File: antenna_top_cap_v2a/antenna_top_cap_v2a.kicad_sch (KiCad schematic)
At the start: 56 parts, among them IC1 PCT2075DP,118, J1 Battery Charge Bypass, J10 BM04B-SRSS-TB(LF)(SN), J12 BM04B-SRSS-TB(LF)(SN), J12 FC Board Connector, J14 BM04B-SRSS-TB(LF)(SN), J16 BM04B-SRSS-TB(LF)(SN), J19 EPS Board Connector, J2 EPS USB Bootselect Jumper, J20 FC USB Bootselect Jumper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

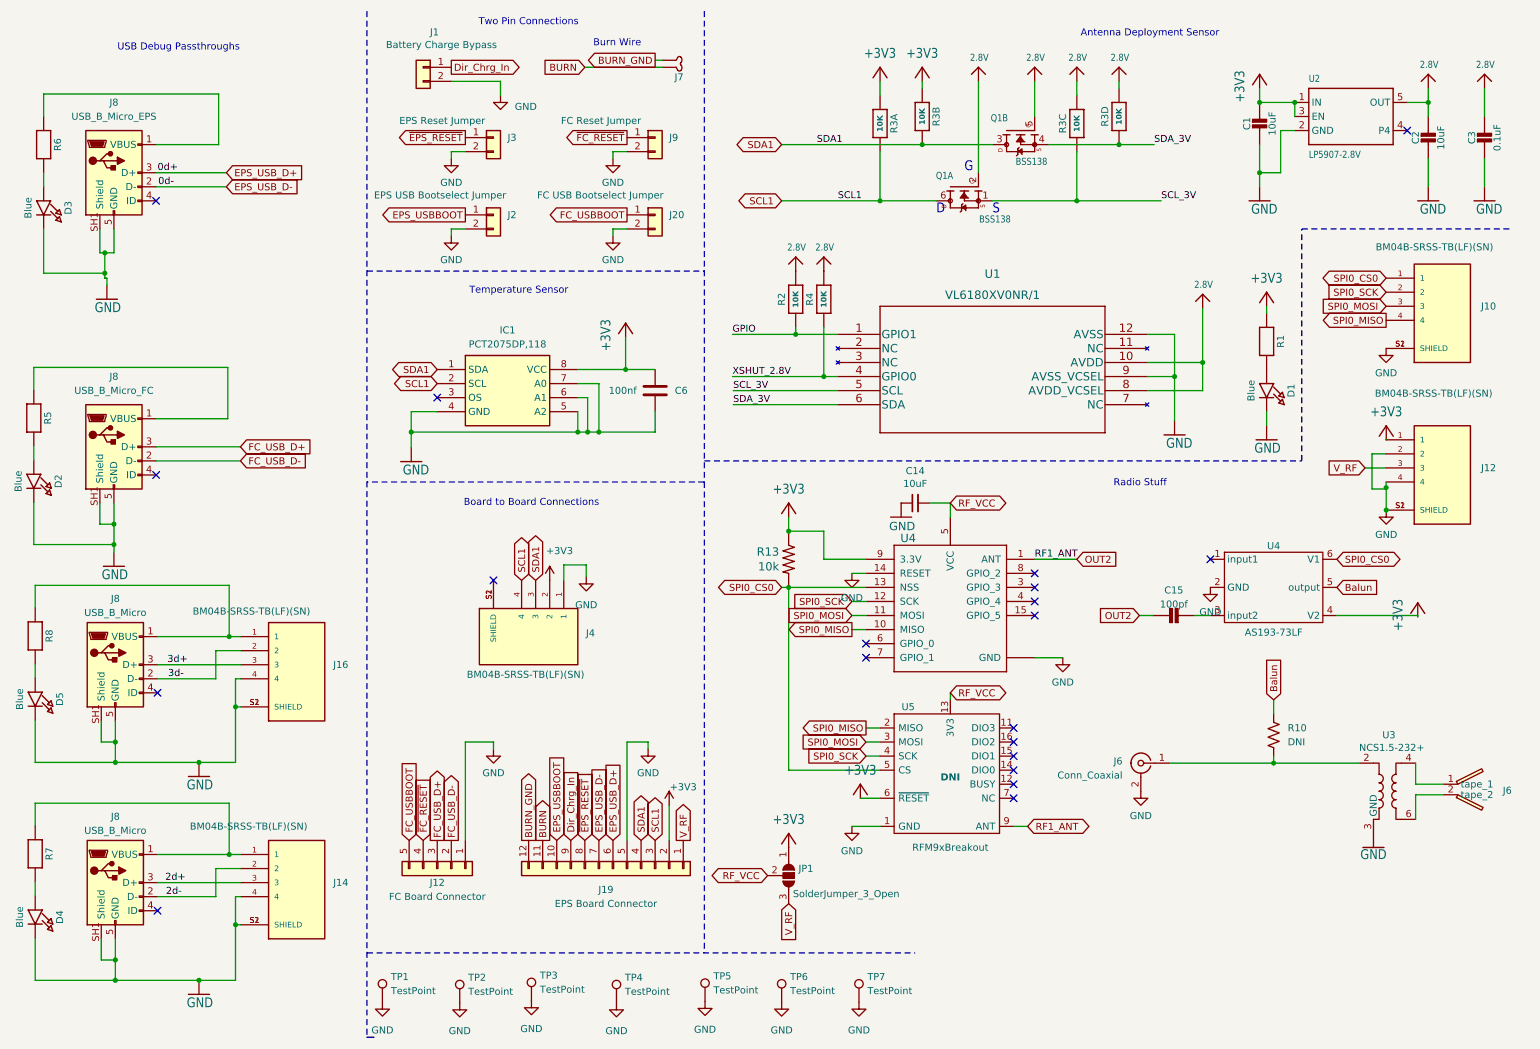
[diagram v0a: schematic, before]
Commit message: Deleted Unused Parts
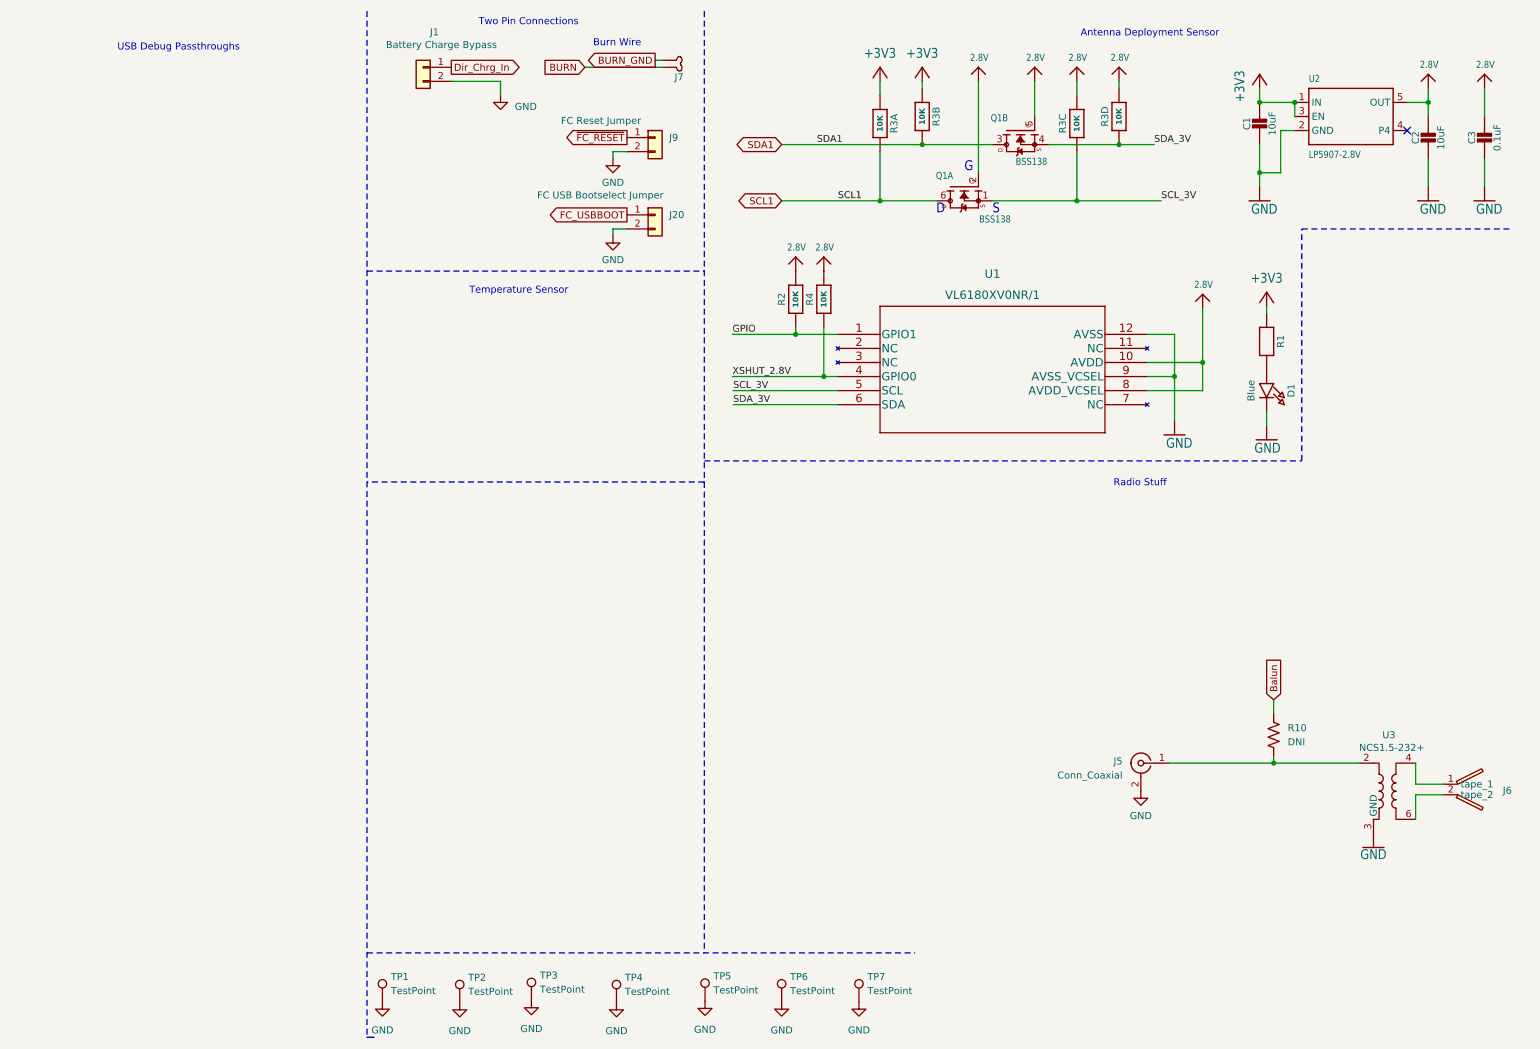
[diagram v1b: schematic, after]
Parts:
- removed C14: 10uF, Capacitor_SMD:C_0603_1608Metric, symbol Device:C_Small
- removed C15: 100pf, Capacitor_SMD:C_0603_1608Metric, symbol Adafruit ItsyBitsy RP2040-eagle-import:CAP_CERAMIC_0402NO
- removed C6: 100nf, Capacitor_SMD:C_0603_1608Metric, symbol Device:C
- removed D2, D3, D4, D5: Blue, LED_SMD:LED_0603_1608Metric, symbol Adafruit ItsyBitsy RP2040-eagle-import:LED0603_NOOUTLINE
- removed IC1: PCT2075DP,118, Package_SO:TSSOP-8_3x3mm_P0.65mm, symbol Antenna:PCT2075DP,118
- removed J10, J12, J14, J16, J4: BM04B-SRSS-TB(LF)(SN), Antenna_board:JST_BM04B-SRSS-TB(LF)(SN), symbol BM04B-SRSS-TB_LF__SN_:BM04B-SRSS-TB(LF)(SN)
- removed J12: FC Board Connector, FC_DEV_BOARD:MOLEX_5040500591, symbol Max_Lib:Connector_Generic_Conn_01x05
- removed J19: EPS Board Connector, Connector_Molex:Molex_Pico-Lock_504050-1291_1x12-1MP_P1.50mm_Horizontal, symbol Connector_Generic:Conn_01x12
- removed J2: EPS USB Bootselect Jumper, Connector_PinHeader_2.54mm:PinHeader_1x02_P2.54mm_Vertical, symbol Connector_Generic:Conn_01x02
- removed J3: EPS Reset Jumper, Connector_PinHeader_2.54mm:PinHeader_1x02_P2.54mm_Vertical, symbol Connector_Generic:Conn_01x02
- removed J8: USB_B_Micro_EPS, Antenna_board:MOLEX_105164-0001(round), symbol Connector:USB_B_Micro
- removed J8 (x2): USB_B_Micro, Antenna_board:MOLEX_105164-0001(round), symbol Connector:USB_B_Micro
- removed J8: USB_B_Micro_FC, Antenna_board:MOLEX_105164-0001(round), symbol Connector:USB_B_Micro
- removed JP1: SolderJumper_3_Open, Jumper:SolderJumper-3_P1.3mm_Open_RoundedPad1.0x1.5mm_NumberLabels, symbol Jumper:SolderJumper_3_Open
- removed R13: 10k, Resistor_SMD:R_0603_1608Metric, symbol mainboard:10KOHM-1_10W-1%(0603)0603
- removed R5, R6, R7, R8: 1K, Resistor_SMD:R_0402_1005Metric, symbol Adafruit ItsyBitsy RP2040-eagle-import:RESISTOR_0402NO
- removed U4: AS193-73LF, Package_TO_SOT_SMD:SuperSOT-6, symbol Antenna:RF_Switch
- removed U4: RFM98PW, Antenna_board:RFM98PW, symbol mainboard:RFM98PW
- removed U5: RFM9xBreakout, Antenna_board:HOPERF_RFM95W_SMD, symbol mainboard:RFM9xBreakout
- R1: value 1K -> 10k
- renumbered J6 to J5
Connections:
- no-connect marks 20 -> 1
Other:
- note removed: "Board to Board Connections"

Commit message: Added USB and DF11 Debug Connector
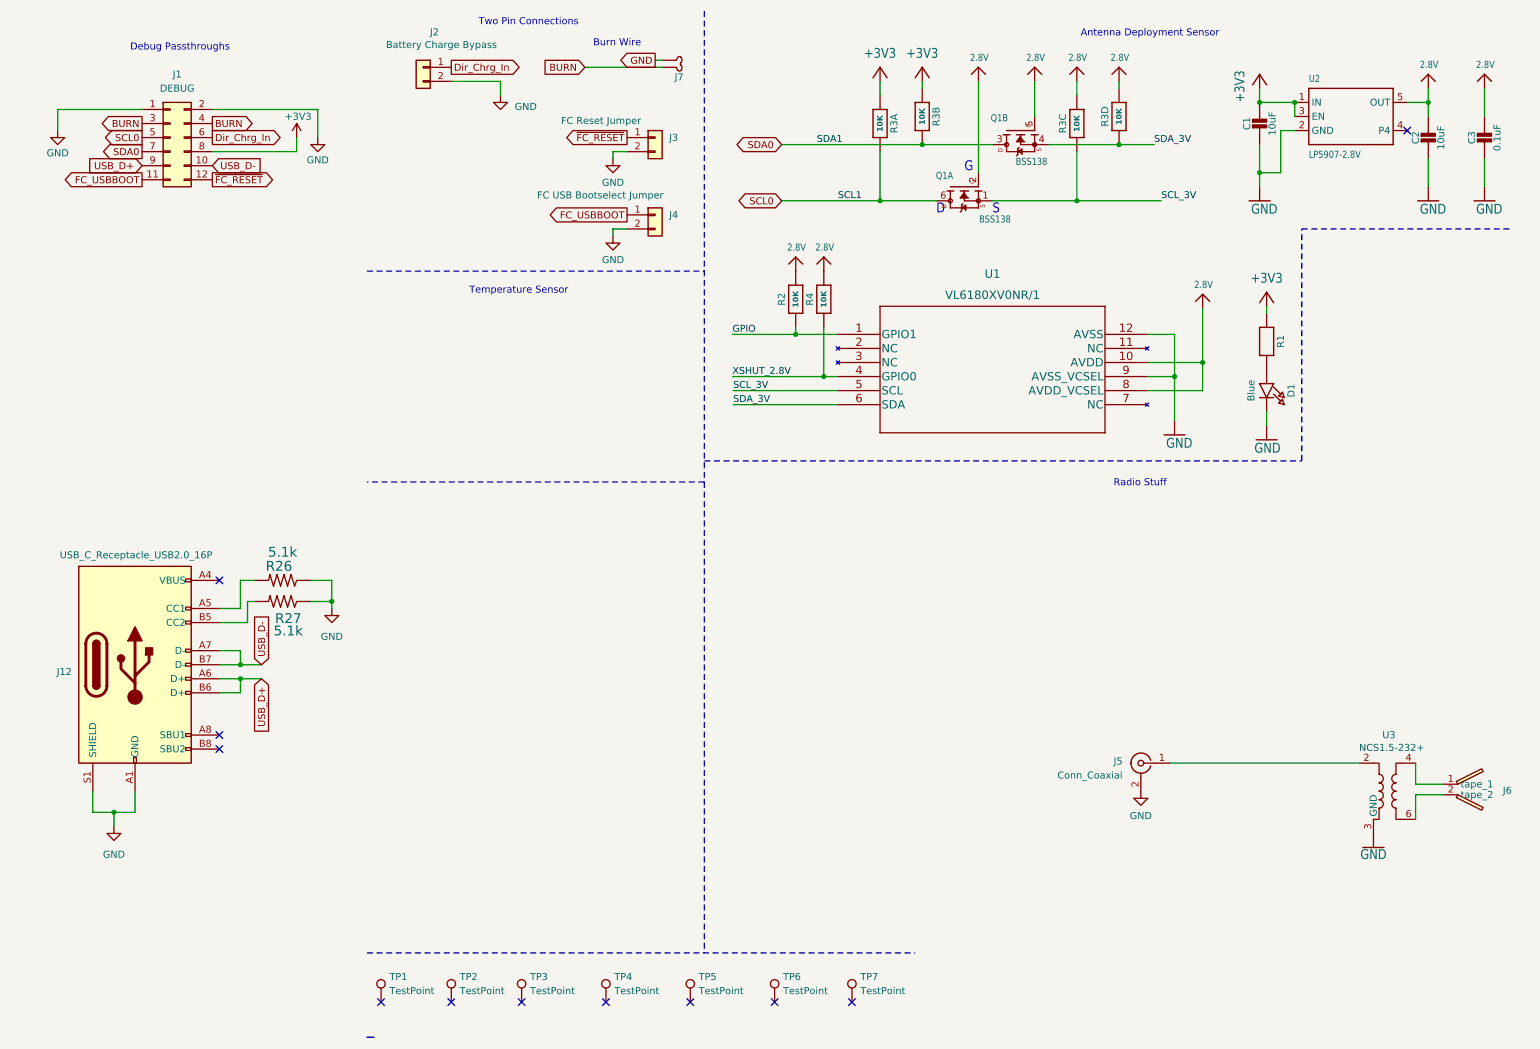
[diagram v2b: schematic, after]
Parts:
- removed R10: DNI, Resistor_SMD:R_0603_1608Metric, symbol Device:R_US
- added J1: DEBUG, Connector_Hirose:Hirose_DF11-12DP-2DSA_2x06_P2.00mm_Vertical, symbol Connector_Generic:Conn_02x06_Odd_Even
- added J12: USB_C_Receptacle_USB2.0_16P, Connector_USB:USB_C_Receptacle_HRO_TYPE-C-31-M-12, symbol Connector:USB_C_Receptacle_USB2.0_16P
- added R26, R27: 5.1k, Resistor_SMD:R_0603_1608Metric, symbol mainboard:RESISTOR0603
- renumbered J1 to J2, J9 to J3, J20 to J4
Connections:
- net BURN_GND is gone; now on net GND: J7.2 (GND)
- net +3V3: now also J1.8 (Pin_8)
- net BURN: now also J1.3 (Pin_3), J1.4 (Pin_4)
- net Dir_Chrg_In: now also J1.6 (Pin_6)
- net FC_USBBOOT: now also J1.11 (Pin_11)
- net GND: now also J1.1 (Pin_1), J1.2 (Pin_2), J12.A1 (GND), J12.A12 (GND), J12.B1 (GND), J12.B12 (GND), J12.S1 (SHIELD), R26.1, R27.1; no longer TP1.1, TP2.1, TP3.1, TP4.1, TP5.1, TP6.1, TP7.1
- net ~{FC_RESET}: now also J1.12 (Pin_12)
- net SCL1 renamed SCL0
- net SCL0: now also J1.5 (Pin_5)
- net SDA1 renamed SDA0
- net SDA0: now also J1.7 (Pin_7)
- new net: J12.A4 (VBUS), J12.A9 (VBUS), J12.B4 (VBUS), J12.B9 (VBUS)
- new net: J12.A5 (CC1), R26.2
- new net: J12.B5 (CC2), R27.2
- new net USB_D+: J1.9 (Pin_9), J12.A6 (D+), J12.B6 (D+)
- new net USB_D-: J1.10 (Pin_10), J12.A7 (D-), J12.B7 (D-)
- no-connect marks 1 -> 11
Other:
- note added: "Debug Passthroughs"
- note removed: "USB Debug Passthroughs"
- moved on the sheet: TP2, TP3, TP4, TP5, TP6, TP7

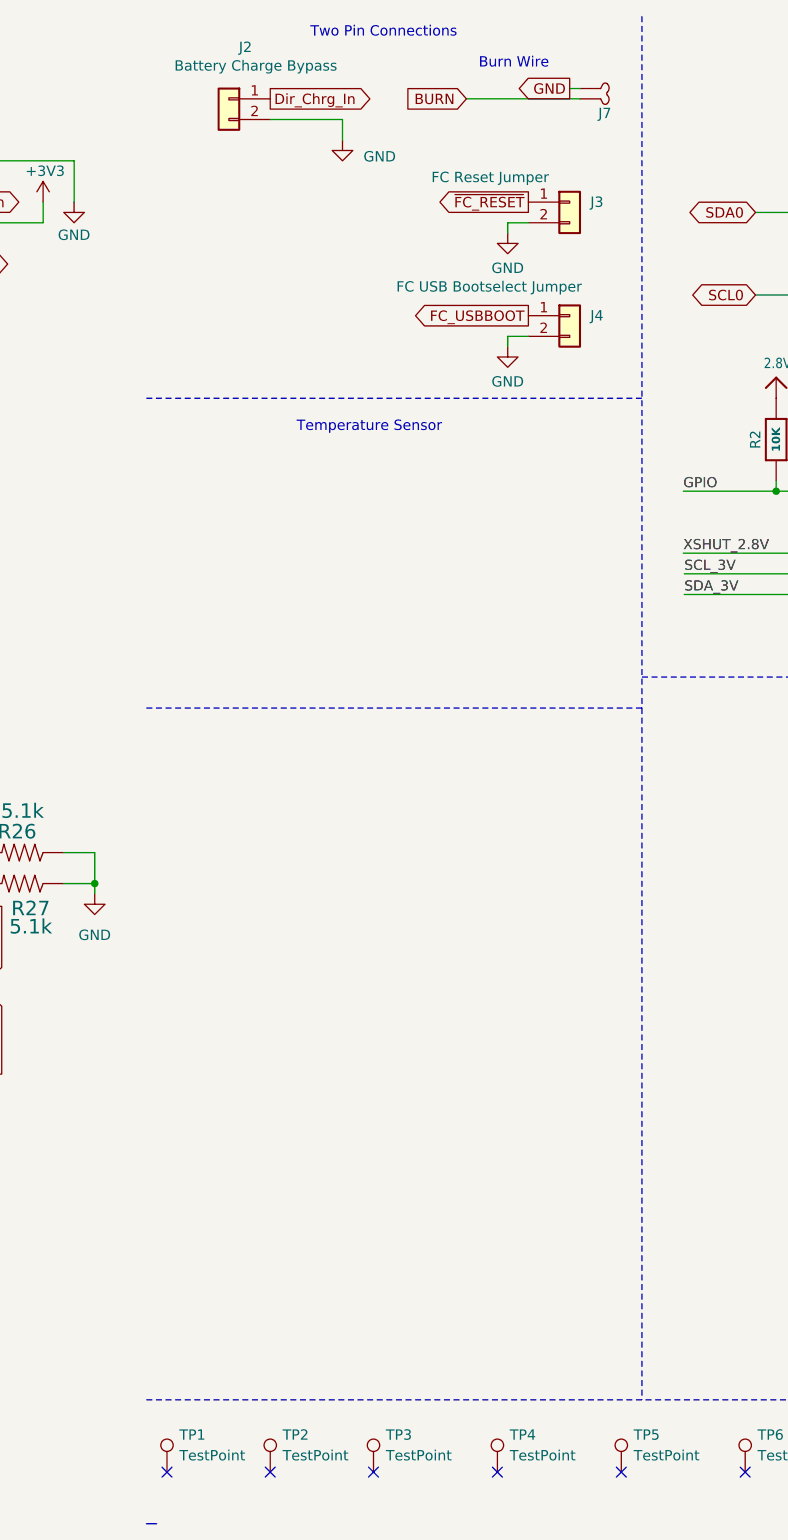
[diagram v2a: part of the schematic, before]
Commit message: Added MCP Temperature Sensor
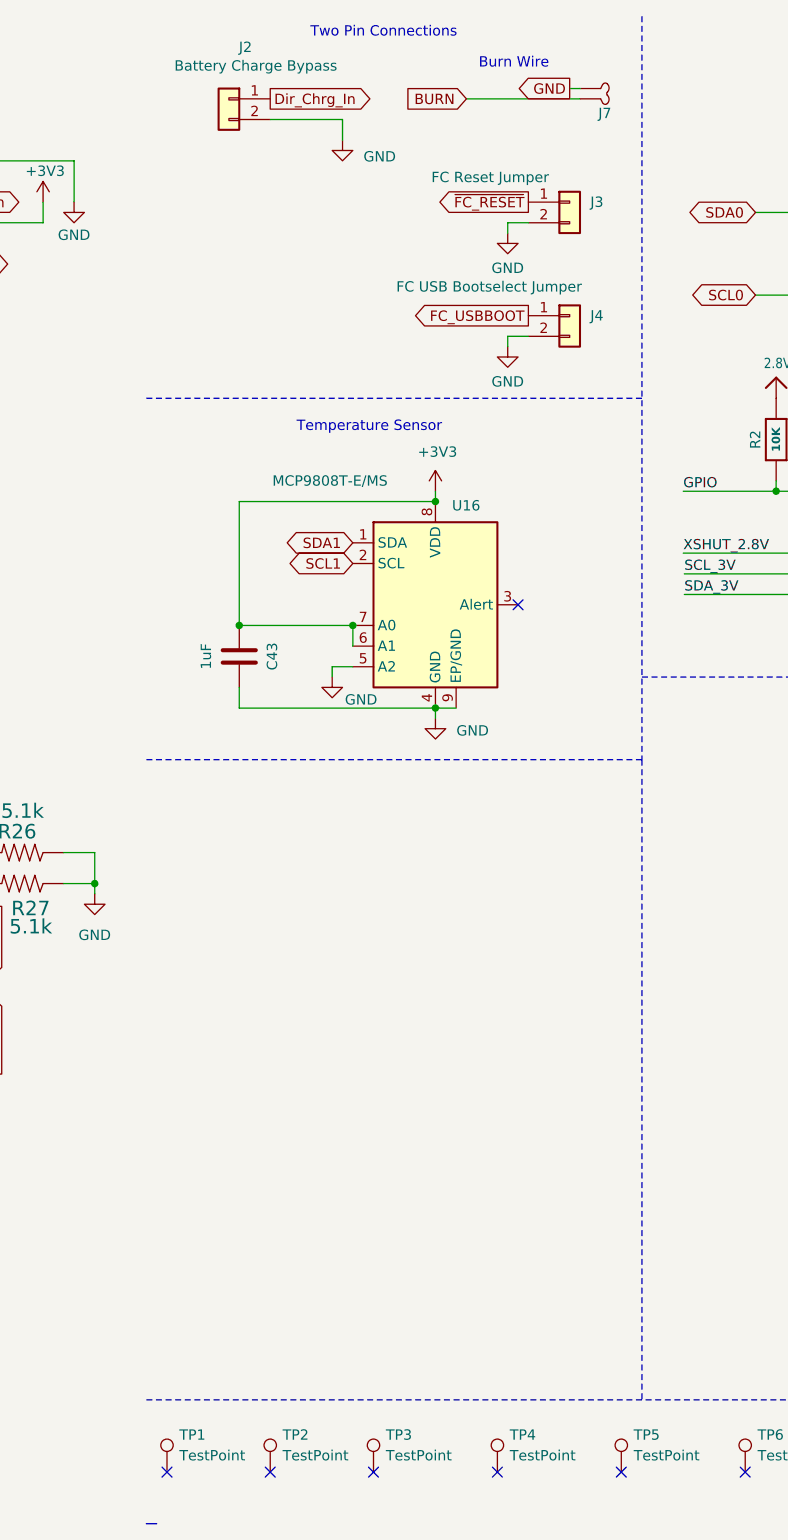
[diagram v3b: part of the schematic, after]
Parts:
- added C43: 1uF, Capacitor_SMD:C_0805_2012Metric, symbol Device:C
- added U16: MCP9808T-E/MS, Package_SO:MSOP-8-1EP_3x3mm_P0.65mm_EP1.5x1.8mm_ThermalVias, symbol Sensor_Temperature:MCP9808_DFN
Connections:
- net +3V3: now also C43.1, U16.6 (A1), U16.7 (A0), U16.8 (VDD)
- net GND: now also C43.2, U16.4 (GND), U16.5 (A2), U16.9 (EP/GND)
- net SCL0: now also U16.2 (SCL)
- net SDA0: now also U16.1 (SDA)
- no-connect marks 11 -> 12
